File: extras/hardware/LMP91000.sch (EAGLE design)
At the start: 10 parts

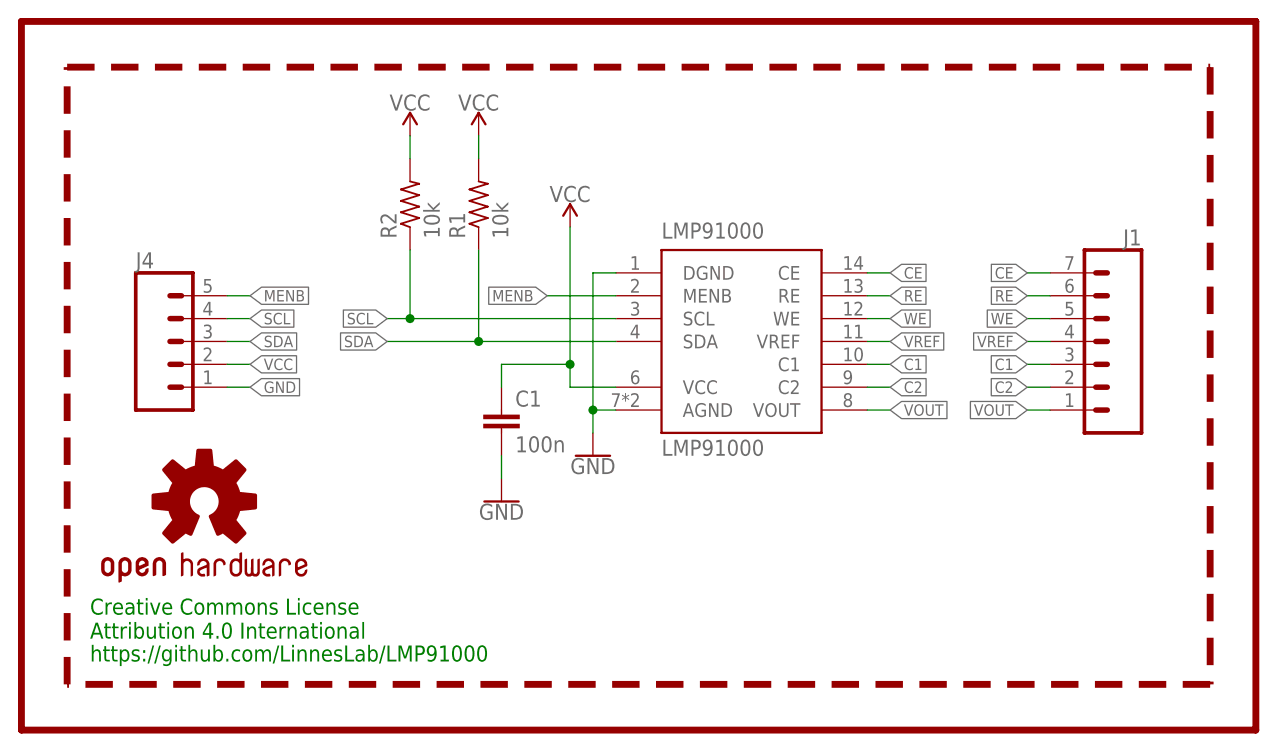
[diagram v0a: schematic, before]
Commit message: Revert "Merge branch 'prototypes' of https://github.com/dzalf/LMP91000"
This reverts commit e035b5a0fbbc45ae6f48cbcd6f64b0519b6adfd6, reversing
changes made to 54f55630fa06b4778207c438d5379e7088d27feb.
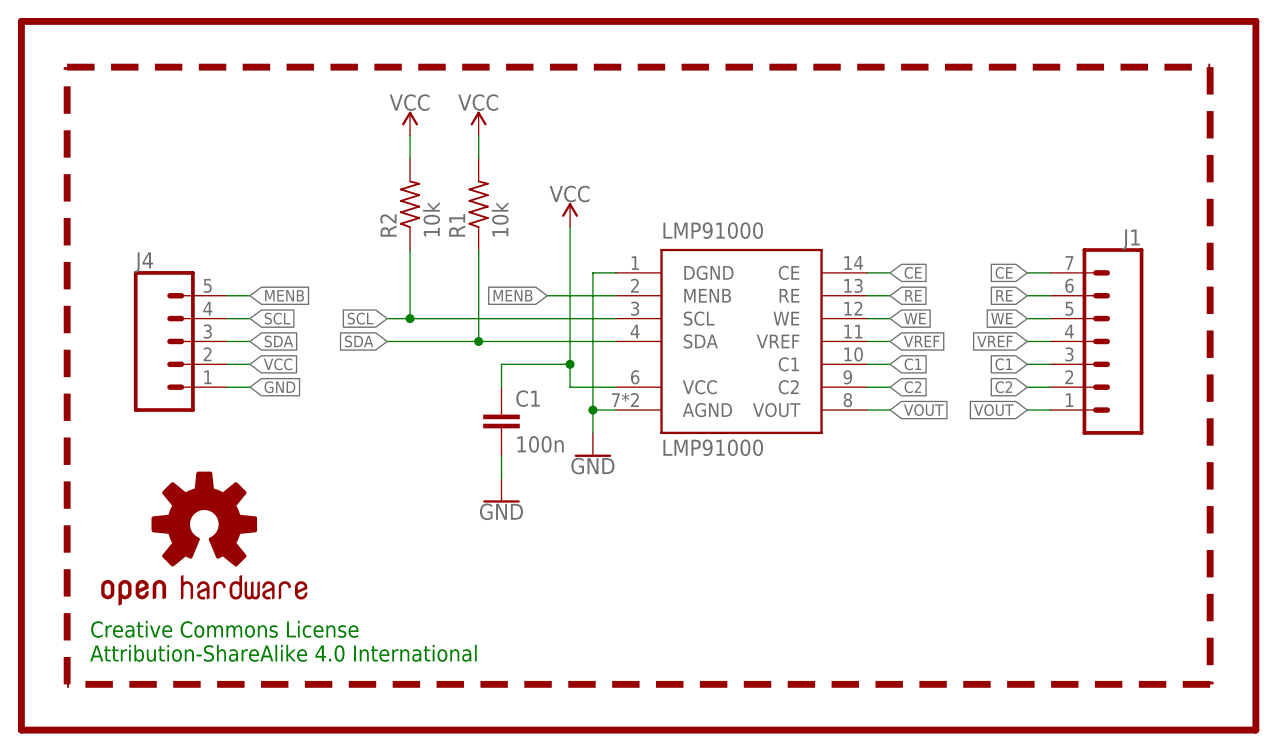
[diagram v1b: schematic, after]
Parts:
- C1: device LinnesLab-Passives:CAPACITOR0402 -> CalvEngIO-Passives:CAPACITOR0402
- J1: device LinnesLab-Connectors:CONN_07NO_SILK -> CalvEngIO-Connectors:CONN_07NO_SILK
- J4: device LinnesLab-Connectors:CONN_05NO_SILK -> CalvEngIO-Connectors:CONN_05NO_SILK
- LMP91000: device LinnesLab-Sensors:LMP91000 -> CalvEngIO-Sensors:LMP91000
- LOGO1: device LinnesLab-Logos:OSHW-LOGOS -> CalvEngIO-Logos:OSHW-LOGOS
- R1, R2: device LinnesLab-Passives:RESISTOR0402-BIGGER -> CalvEngIO-Passives:RESISTOR0402
- U$1: device LinnesLab-Logos:LINNES.LAB.05 -> CalvEngIO-Logos:LINNES.LAB.05
- U$2: device LinnesLab-Logos:LINNES.LAB.LOGO -> CalvEngIO-Logos:LINNES.LAB.LOGO
- U$3: device LinnesLab-Logos:REVISION.B -> CalvEngIO-Symbols:REVISION.B
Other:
- note added: "Creative Commons License Attribution-ShareAlike 4.0 International"
- note removed: "Creative Commons License Attribution 4.0 International"
- note removed: "https://github.com/LinnesLab/LMP91000"
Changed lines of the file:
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@@
 <?xml version="1.0" encoding="utf-8"?>
 <!DOCTYPE eagle SYSTEM "eagle.dtd">
-<eagle version="9.2.2">
+<eagle version="8.4.2">
 <drawing>
 <settings>
@@
 </classes>
 <parts>
-<part name="LMP91000" library="LinnesLab-Sensors" deviceset="LMP91000" device=""/>
+<part name="LMP91000" library="CalvEngIO-Sensors" deviceset="LMP91000" device=""/>
 <part name="GND1" library="CalvEngIO-Symbols" deviceset="GND" device=""/>
 <part name="SUPPLY1" library="CalvEngIO-Symbols" deviceset="VCC" device=""/>
-<part name="C1" library="LinnesLab-Passives" deviceset="CAPACITOR" device="0402" value="100n"/>
+<part name="C1" library="CalvEngIO-Passives" deviceset="CAPACITOR" device="0402" value="100n"/>
 <part name="GND2" library="CalvEngIO-Symbols" deviceset="GND" device=""/>
-<part name="R1" library="LinnesLab-Passives" deviceset="RESISTOR" device="0402-BIGGER" value="10k"/>
-<part name="R2" library="LinnesLab-Passives" deviceset="RESISTOR" device="0402-BIGGER" value="10k"/>
+<part name="R1" library="CalvEngIO-Passives" deviceset="RESISTOR" device="0402" value="10k"/>
+<part name="R2" library="CalvEngIO-Passives" deviceset="RESISTOR" device="0402" value="10k"/>
 <part name="SUPPLY3" library="CalvEngIO-Symbols" deviceset="VCC" device=""/>
 <part name="SUPPLY4" library="CalvEngIO-Symbols" deviceset="VCC" device=""/>
-<part name="J4" library="LinnesLab-Connectors" deviceset="CONN_05" device="NO_SILK"/>
-<part name="LOGO1" library="LinnesLab-Logos" deviceset="OSHW-LOGO" device="S"/>
-<part name="J1" library="LinnesLab-Connectors" deviceset="CONN_07" device="NO_SILK"/>
-<part name="U$2" library="LinnesLab-Logos" deviceset="LINNES.LAB.LOGO" device=""/>
-<part name="U$1" library="LinnesLab-Logos" deviceset="LINNES.LAB" device=".05"/>
-<part name="U$3" library="LinnesLab-Logos" deviceset="REVISION.B" device=""/>
+<part name="J4" library="CalvEngIO-Connectors" deviceset="CONN_05" device="NO_SILK"/>
+<part name="LOGO1" library="CalvEngIO-Logos" deviceset="OSHW-LOGO" device="S"/>
+<part name="J1" library="CalvEngIO-Connectors" deviceset="CONN_07" device="NO_SILK"/>
+<part name="U$2" library="CalvEngIO-Logos" deviceset="LINNES.LAB" device=".LOGO"/>
+<part name="U$1" library="CalvEngIO-Logos" deviceset="LINNES.LAB" device=".05"/>
+<part name="U$3" library="CalvEngIO-Symbols" deviceset="REVISION.B" device=""/>
 </parts>
 <sheets>
 <sheet>
 <plain>
-<text x="12.7" y="12.7" size="1.778" layer="91">Creative Commons License
-Attribution 4.0 International</text>
+<text x="12.7" y="10.16" size="1.778" layer="91">Creative Commons License
+Attribution-ShareAlike 4.0 International</text>
 <text x="10.16" y="83.82" size="3.81" layer="90" font="vector" ratio="15">LMP91000 Breakout Board</text>
 <wire x1="10.16" y1="76.2" x2="137.16" y2="76.2" width="0.762" layer="94" style="longdash"/>
@@
 <wire x1="142.24" y1="2.54" x2="5.08" y2="2.54" width="0.762" layer="94"/>
 <wire x1="5.08" y1="2.54" x2="5.08" y2="81.28" width="0.762" layer="94"/>
-<text x="12.7" y="10.16" size="1.778" layer="91">https://github.com/LinnesLab/LMP91000</text>
 </plain>
 <instances>
-<instance part="LMP91000" gate="G$1" x="83.82" y="50.8" smashed="yes">
-<attribute name="NAME" x="76.2" y="57.15" size="1.778" layer="95"/>
-</instance>
-<instance part="GND1" gate="1" x="68.58" y="33.02" smashed="yes">
-<attribute name="VALUE" x="68.58" y="32.766" size="1.778" layer="96" align="top-center"/>
-</instance>
-<instance part="SUPPLY1" gate="G$1" x="66.04" y="58.42" smashed="yes">
-<attribute name="VALUE" x="66.04" y="61.214" size="1.778" layer="96" align="bottom-center"/>
-</instance>
-<instance part="C1" gate="G$1" x="58.42" y="35.56" smashed="yes">
-<attribute name="NAME" x="59.944" y="38.481" size="1.778" layer="95"/>
-<attribute name="VALUE" x="59.944" y="33.401" size="1.778" layer="96"/>
-</instance>
-<instance part="GND2" gate="1" x="58.42" y="27.94" smashed="yes">
-<attribute name="VALUE" x="58.42" y="27.686" size="1.778" layer="96" align="top-center"/>
-</instance>
-<instance part="R1" gate="G$1" x="55.88" y="60.96" smashed="yes" rot="R90">
-<attribute name="NAME" x="54.3814" y="57.15" size="1.778" layer="95" rot="R90"/>
-<attribute name="VALUE" x="59.182" y="57.15" size="1.778" layer="96" rot="R90"/>
-</instance>
-<instance part="R2" gate="G$1" x="48.26" y="60.96" smashed="yes" rot="R90">
-<attribute name="NAME" x="46.7614" y="57.15" size="1.778" layer="95" rot="R90"/>
-<attribute name="VALUE" x="51.562" y="57.15" size="1.778" layer="96" rot="R90"/>
-</instance>
-<instance part="SUPPLY3" gate="G$1" x="55.88" y="68.58" smashed="yes">
-<attribute name="VALUE" x="55.88" y="71.374" size="1.778" layer="96" align="bottom-center"/>
-</instance>
-<instance part="SUPPLY4" gate="G$1" x="48.26" y="68.58" smashed="yes">
-<attribute name="VALUE" x="48.26" y="71.374" size="1.778" layer="96" align="bottom-center"/>
-</instance>
-<instance part="J4" gate="G$1" x="20.32" y="45.72" smashed="yes">
-<attribute name="VALUE" x="17.78" y="35.814" size="1.778" layer="96" font="vector"/>
-<attribute name="NAME" x="17.78" y="53.848" size="1.778" layer="95" font="vector"/>
-</instance>
-<instance part="LOGO1" gate="G$1" x="25.4" y="27.94" smashed="yes"/>
-<instance part="J1" gate="G$1" x="124.46" y="43.18" smashed="yes" rot="MR0">
-<attribute name="VALUE" x="129.54" y="33.274" size="1.778" layer="96" font="vector" rot="MR0"/>
-<attribute name="NAME" x="129.54" y="56.388" size="1.778" layer="95" font="vector" rot="MR0"/>
-</instance>
-<instance part="U$2" gate="G$1" x="96.52" y="20.32" smashed="yes"/>
-<instance part="U$1" gate="G$1" x="96.52" y="15.24" smashed="yes"/>
-<instance part="U$3" gate="G$1" x="91.44" y="83.82" smashed="yes"/>
+<instance part="LMP91000" gate="G$1" x="83.82" y="50.8"/>
+<instance part="GND1" gate="1" x="68.58" y="33.02"/>
+<instance part="SUPPLY1" gate="G$1" x="66.04" y="58.42"/>
+<instance part="C1" gate="G$1" x="58.42" y="35.56"/>
+<instance part="GND2" gate="1" x="58.42" y="27.94"/>
+<instance part="R1" gate="G$1" x="55.88" y="60.96" rot="R90"/>
+<instance part="R2" gate="G$1" x="48.26" y="60.96" rot="R90"/>
+<instance part="SUPPLY3" gate="G$1" x="55.88" y="68.58"/>
+<instance part="SUPPLY4" gate="G$1" x="48.26" y="68.58"/>
+<instance part="J4" gate="G$1" x="20.32" y="45.72"/>
+<instance part="LOGO1" gate="G$1" x="25.4" y="25.4"/>
+<instance part="J1" gate="G$1" x="124.46" y="43.18" rot="MR0"/>
+<instance part="U$2" gate="G$1" x="96.52" y="20.32"/>
+<instance part="U$1" gate="G$1" x="96.52" y="15.24"/>
+<instance part="U$3" gate="G$1" x="91.44" y="83.82"/>
 </instances>
 <busses>
